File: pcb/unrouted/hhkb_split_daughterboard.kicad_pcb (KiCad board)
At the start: 2 copper layers, 21 x 32 mm, 11 parts

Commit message: 行のネット名を「ケーブル上の位置」にし、行の並びを左右で別々に決めた
利用者の指摘「左右で ROW の順番を変えてもいい（左右で違う FW になるのは
確定している）。そういう意味で、DB の ROWx というピン名前付は不適切に
なるかもしれません」。理由は「左右 MAIN PCB を可能な限り鏡像にしている
がゆえに、どの FFC ピンがどの行に最適かが変わってくる」。

**ネット名を ROW0..4 → ROW_A..E に改めた。**名前が指すのは行番号ではなく
**ケーブル上の位置**（子基板のレーン）。行番号を名前にすると、左右で違う
行を同じ線に載せた瞬間に嘘になる（左の ROW2 が右では行 4 を運ぶ）。

**`row-gpios` を共通の dtsi から左右の overlay へ移した。**行がどの GPIO に
来るかは左右で物理的に違う——J_DB が左は板の右端・右は左端にあり、同じ
FFC のピンでも行バスへ近づく向きが逆。共通に 1 つだけ書くと、どちらかの
基板で必ず交差が出る。`matrix.row_nets(half)` が唯一の出所になった。

**割り当ての考え方も利用者の指摘で組み直した。**当初は「上へ行く群／下へ
行く群」で交差を数えていたが、正しくは **J_DB から遠い行ほど、パッド列で
「板の内側」の枠へ**。遠くまで行く枝を内側に置くと他の枝を跨がずに列を
離れられる。左右で並びが逆になる（12 番の板端／内側の意味が入れ替わる）。

    左: 行4=ROW_E 行3=ROW_D 行0=ROW_C 行2=ROW_B 行1=ROW_A
    右: 行4=ROW_A 行3=ROW_B 行0=ROW_C 行2=ROW_D 行1=ROW_E

**3 基板とも DRC 違反 0 / 未配線 0。**逆向きだと左 1 本・右 3 本が未配線に
なることを実測した（総当たりのモデルだけでは決まらなかった）。

検査は新しい構造に合わせて書き換え、**故意に壊して落ちることを確認した**
（overlay のピンを 1 つ変える／行を 2 つ入れ替える）。「左右で並びが違って
よい」ことも検査に書いて、揃える方向の変更が入らないようにした。

⚠️ 主基板の SPARE/SPARE2 が片側 1 ピンなので test_circuit が 2 件赤。
これは左右基板の残作業（J_DB の予備ピンの行き先）で解消する。

Co-Authored-By: Claude Opus 5 (1M context) <noreply@anthropic.com>
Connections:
- net ROW0 renamed ROW_E
- net ROW1 renamed ROW_C
- net ROW2 renamed ROW_D
- net ROW3 renamed ROW_A
- net ROW4 renamed ROW_B

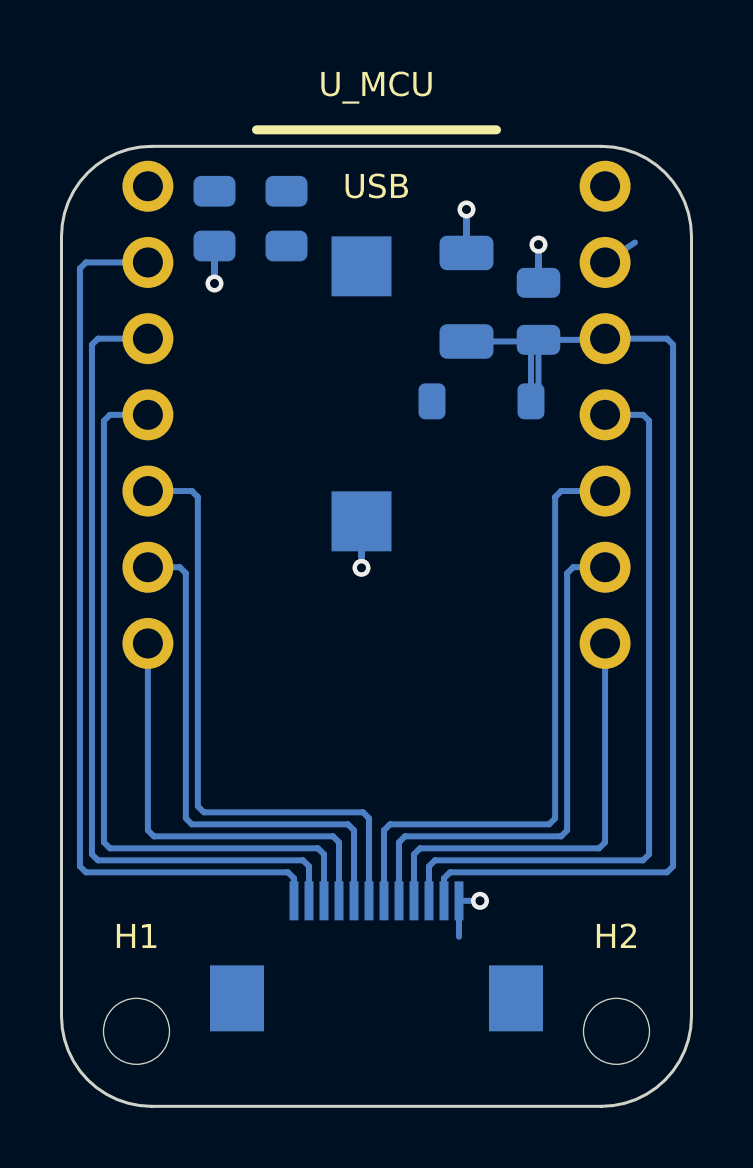
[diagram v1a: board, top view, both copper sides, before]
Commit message: 子基板の未配線 4 件を消し、GND スタブの重複とシルクを直した
**未配線 4 件（VBATT_SW / VBATT_SENSE）の正体は Freerouting への入力だった。**
DSN に `(autoroute_settings)` があるだけで、Freerouting 2.3.0 が子基板の
ネットを 1 本も見なくなる。同じ DSN でブロックの有無だけを変えた実測:

    あり … "started with 0 unrouted nets" / SES 18 行（空）
    なし … "started with 4 unrouted nets" / SES 98 行

中身は関係ない（fanout / start_ripup_costs / layer_rule を 4 通り試して
すべて 0）。4 接続は直線経路に障害物が無く（2.2〜4.0mm・邪魔なし）、
「密集して引けない」のではなく**渡っていなかった**。子基板だけ外す。
主基板は正常に働く（左 started_with=60）ので残す。

**GND の引き出しが 1 パッドに 2 本生えていた**（利用者「GND は同じベタに
2 つ生えています。両方いるか、という事です」）。`_prewire_power` と
`gnd_fanout.place` がどちらも同じパッドから B.Cu へ出るため、6 パッドに
11 本。うち 4 組は始点も向きも同じで、1.2mm 側はビアへ向かうスタブの
完全な部分区間だった。ビアで受けるパッドには引かない。

さらに **U_MCU の GND は PTH**（穴 1.0mm）で、穴自体が両面のベタを貫く
ので引き出しは元から不要だった。「最寄りビアまで 3.22mm」と書いたのは
スタブの端から測った誤りで、中心からは 2.13mm。そもそも距離の問題では
なかった。引き出しは 11 本 → 0 本になり、未配線は増えていない。

**肩の高さを左右で揃えた**（利用者「この微妙に高さ違うのを直してほしい」）。
`over` を `i`（この列の何本目か）ではなく `slot`（枠の番号）で数える。
本数の違う列で同じ役割の線が違う高さになっていた。交差は増えない
（全 11 ネットを総当たりで交差判定して 0 件）。V3V3 だけは鏡像にならないが
利用者の判断で現状維持。

**V3V3 の往復を消した**（利用者「C_DB と D_PWR の間で不要に 2 本」）。
x 順の鎖に、一列から 2mm 下がった D_PWR が挟まって往復していた。
横一列のものだけで鎖を作り、外れたものは最寄りへ 1 本。

**ビアの空白を埋めた**（利用者「D6, D7 の下の領域、GND とビア打てないの？」）。
格子は λ/10 = 6.5mm と粗く、21x32mm では格子点が十数個しかないので
1 点が塞がると周りが丸ごと空く。実測で打てる点が 168 箇所あったのに
0 個だった。ピッチは動かさず、外れた点だけ半ピッチ以内で探し直す。
格子 7 → 14 個。

**シルクは利用者が KiCad で並べたものを出所にする**（`POWER_PLACE` と同じ）。
4 方向を試して空きを探す実装を書いたが、判定を厳しくするほど
「どこも当たる＝動かさない」が増え、13 → 10 → 13 → 15 件と悪化した。
機械的な 4 方向では解が無い。`SILK_REF` に固定し、並べ直したときは
`_read_silk_from` で吸い出す（手で書き写さない）。

R_HI / SW_PWR の配置も利用者の基板から読み直した（11 部品すべて一致）。

子基板: 違反 0 / 未配線 0 / 警告 13 → 5。基板の検査 90 件通過。

Co-Authored-By: Claude Opus 5 (1M context) <noreply@anthropic.com>
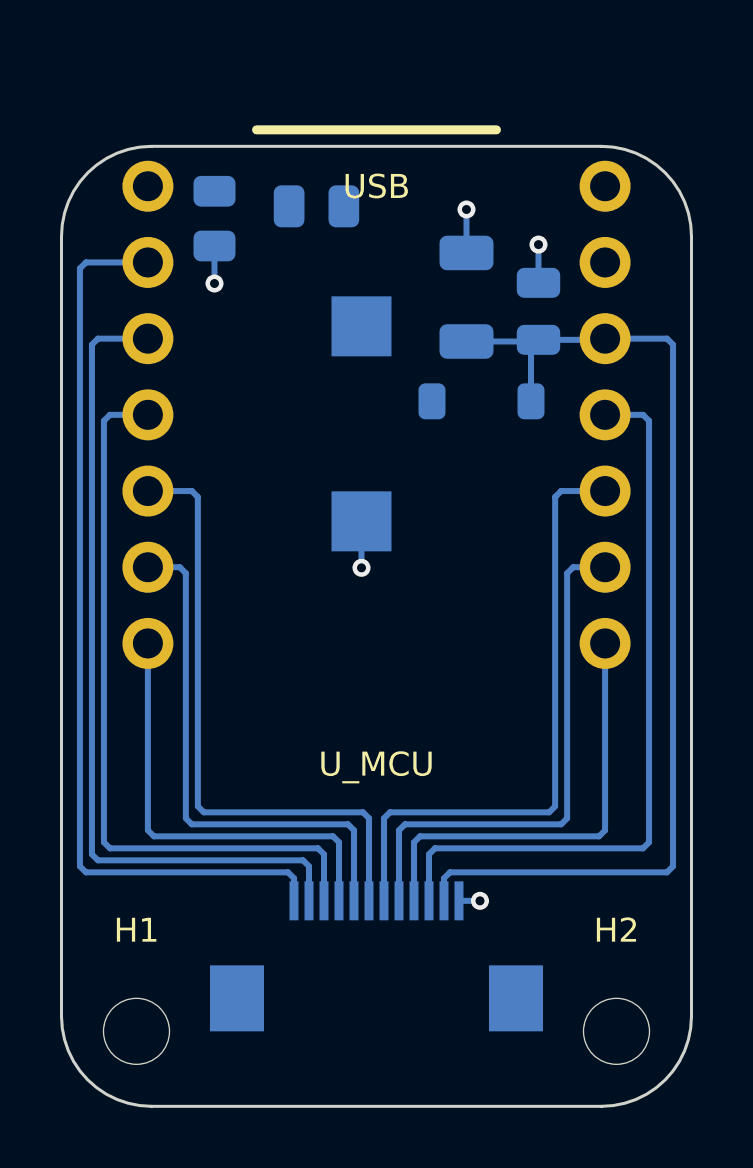
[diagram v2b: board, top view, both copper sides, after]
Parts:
- moved SW_PWR_1 2.00 mm to (149.5, 90.0)
- moved R_HI 1.08 mm to (148.0, 86.0), turned to 180 degrees
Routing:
- net GND: track 13.4 -> 6.23 mm
- net V3V3: track 37.0 -> 35.3 mm

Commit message: 子基板のアンテナ禁止域を 3.5 角から 7.5 角へ広げ、配線とビアも禁止した
アンテナの実体の四方に 2.0mm の逃げを取る。ベタだけでなく配線とビアも
禁止する（両面）。3 基板とも DRC 違反 0・未配線 0。

**2.0mm の出所**: 4 方向を同時に広げて信号配線・パッドに当たらない上限が
2.2mm（pcb/unrouted/ の板で実測）。そこから 0.2mm 引いた。
Seeed が XIAO 上で確保している 1.76mm を上回る——ただし**これは公開仕様
ではない**。wiki・SOM データシート・LCSC を全文検索したが keepout の mm
指定は 1 つも無く、公式 KiCad プロジェクト（V1.1）から実測した値。

**配線とビアを禁止できた理由**: 「FFC から XIAO への 12 本が必ず横切るので
禁止すると 14 件の違反」というコメントは、帯が板の全幅だった頃の記録で、
x 4.5mm に絞った #41 以降は当てはまらない。実測で帯に掛かるものは 0 件。

**gnd_fanout の根本原因も直した**: ビアを置く経路が 2 つある（spots と
stitch）のに、`_obstacles` 側だけがルール領域を見ていた。`spots` は
`_pad_boxes` しか見ないので、パッド直近のファンアウトのビアだけが禁止域に
入り、DRC が items_not_allowed を 1 件出した。両方に入れ、かつ**ビアの
外径ぶん膨らませる**（判定側が見るのはビアの中心なので、箱のままだと
中心が外なら通って銅が中に入る）。

検査は y 方向の拡大が無検査だった穴を塞いだ（逃げを 0 にしても 13 件
全部が通っていた）。故意に壊して落ちることを確認済み。禁止内容
（tracks/vias/copperpour が not_allowed か）も見るようにした。

⚠️ **未解決**: 禁止域が XIAO の中心から左に 1.9mm ずれて見える。
`ANTENNA_X = -1.9` の符号を実機で裏取りできていない（interface.py 自身が
「裏返すと左右が入れ替わり結論が逆になる」と警告している値）。

pytest tools は未実行（test_daughterboard.py の 13 件のみ通過を確認）。

Co-Authored-By: Claude Opus 5 (1M context) <noreply@anthropic.com>
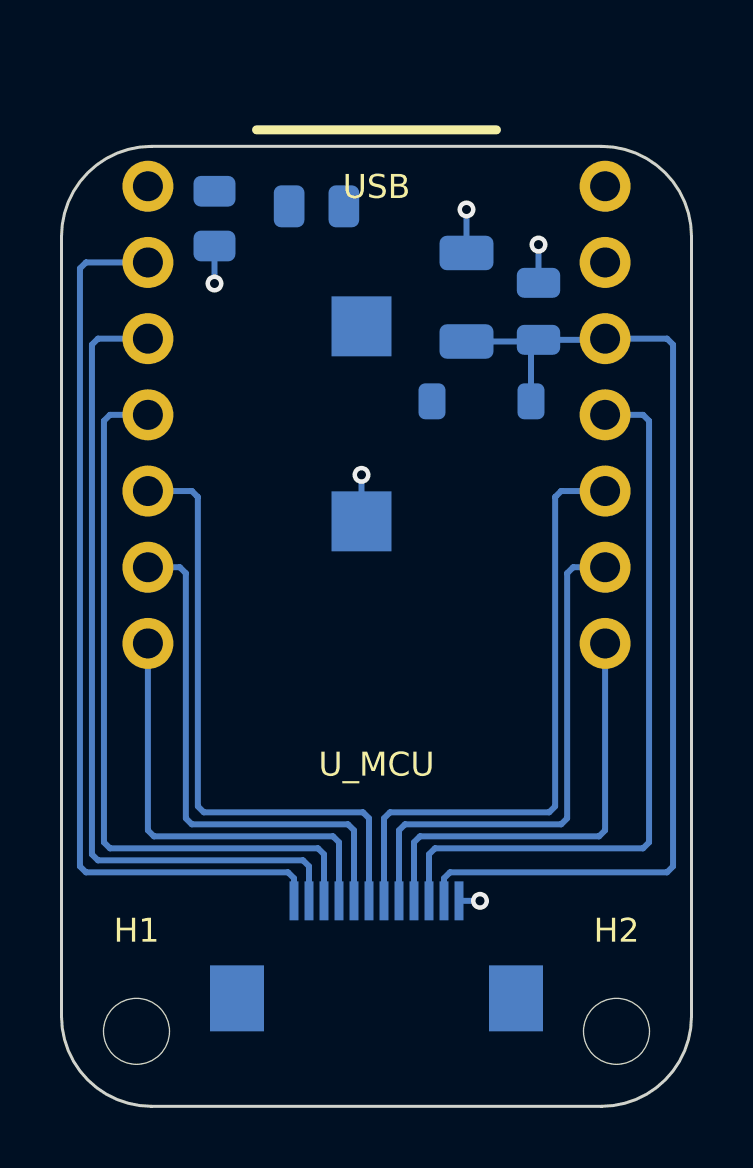
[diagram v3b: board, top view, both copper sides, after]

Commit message: 子基板のシルク位置を利用者の配置で確定させた（silk_overlap 5 → 0）
参照名のラベルが自分の部品の外形線に近すぎる警告が 5 件残っていた。
利用者が KiCad で 9 個を並べ直し、SILK_REF をその基板から
_read_silk_from で吸い出して更新した（手で書き写していない）。

子基板は 違反 0 / 未配線 0 / 警告 0。gen_daughterboard → autoroute で
再生成しても同じ配置が出ることを確認した。

⚠️ この更新には検査が付いていない。SW_PWR_1 を古い座標に戻して
再生成しても DRC は 0 件のままで、silk_overlap の再発を検出できない
（未配線基板では silk_overlap が常に 0 だった）。仕組みではなく
コメントの注意書きに頼っている。

なお .kicad_pro の solder_mask_to_copper_clearance が 0.005 に
なっていたのを 0.0 へ戻した（3 基板で揃った）。利用者は意図していない。

Co-Authored-By: Claude Opus 5 (1M context) <noreply@anthropic.com>
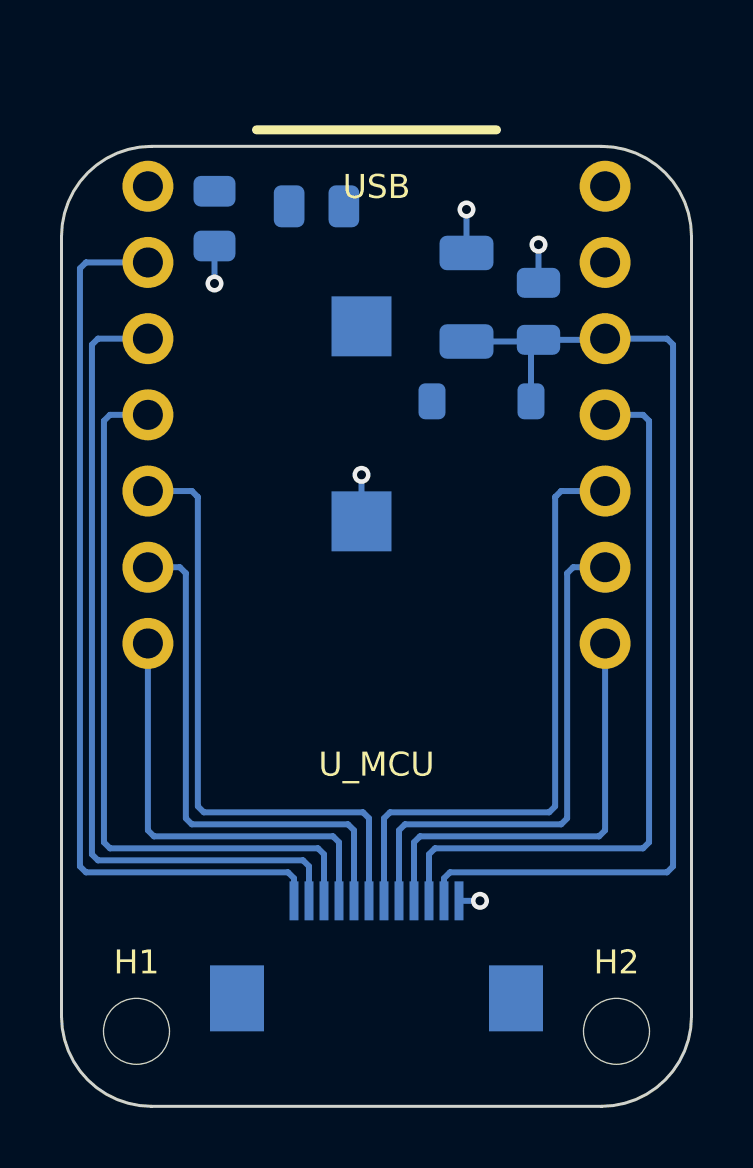
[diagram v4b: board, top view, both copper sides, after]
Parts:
- D_PWR: value schottky -> B5819W
- R_HI, R_LO: value res_1M -> 1M

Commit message: バルクコンデンサを削除した（実測で不要と判明・#44）
C_BULK（100µF・C15008・1206）を子基板から消した。実装部品が 2 個減る。
消したのはバルクだけで、パスコン（C_DB / C_U1 / C_U2）は全部残る。

判断の根拠は 2026-08-16 の実測（DS1104Z・シャント 10Ω ローサイド）。
それまで根拠だった BLE_TX_CURRENT = 15mA は出典の無い推定値で、
provisional-values にも「未測定」と書いてあった。

  BLE の最大瞬間風速  10.22mA（広告とスキャンの重なり込み）
  降下 = 10.22mA × 9.2Ω = 94mV   ← 容量ゼロでもこれが上限
  余裕 300mV に対して 31%（安全率 3.2 倍）
  µs 級の尖り  1ns 分解能・60 万点を全数走査して 0 個

降下は「電流 × 内部抵抗」で決まりコンデンサでは消せない、という点は
前から正しかった。間違っていたのは電流の値のほう。そして µs 級の尖りが
無かったので、「µs 級の電流変動を supply する」というバルクの存在理由が
消えた。守る相手が実在しなかった。

1 回目の測定は SPLIT=n で、広告だけを動かしていた。「ピークの高さは
送信理由によらないはず」という推論で、実測ではなかった。利用者の指摘
「バルクの役割は電流の最大瞬間風速に耐えることでは」で測り直したら
27% 上がった（8.02 → 10.22mA）。TX は PA、スキャンは LNA と別の回路が
動くので、重なると足し算になる。

検査は向きを 180 度変えた。test_there_is_a_bulk_capacitor（在ること）
→ test_the_transmit_droop_needs_no_bulk_capacitor（無くて足りること）。
「バルクが無い」を固定するのではなく、無くてよい条件が成立し続けて
いることを見る。BLE_TX_CURRENT を 0.040 にすると落ちることを確認済み
（破綻点 32.6mA）。変異検査の壊し方も「消す」→「復活させる」に反転。

test_there_is_exactly_one_bulk_capacitor_shared_by_the_board（#38 の番人）
は守る対象を失ったので削除し、跡地に理由を書いた。

基板は再生成して DRC 0/0/0。実基板のフットプリントを列挙して、
C_BULK が無く C_DB が在ることを確認した。1206 が 1 個ぶん空いた。

測定治具（c4_txburst / led_force_off.c）は測定専用なので main に入れず、
meas/c4-txburst ブランチに残す。記録の §5 に置き場所を書いた。

副産物として #44（深いスリープ中に電源を切っても 53 秒消えない）が
解決する。バルクの電荷が抜けないのが原因だったので、数秒になる。

Co-Authored-By: Claude Opus 5 (1M context) <noreply@anthropic.com>
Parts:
- removed C_BULK: 100uF, C_1206_3216Metric
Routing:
- net V3V3: track 35.3 -> 32.8 mm
- net GND: track 6.23 -> 4.78 mm, vias 5 -> 4
